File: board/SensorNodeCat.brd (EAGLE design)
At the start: 45.7 x 24.1 mm, 18 parts, among them J1 JP5E

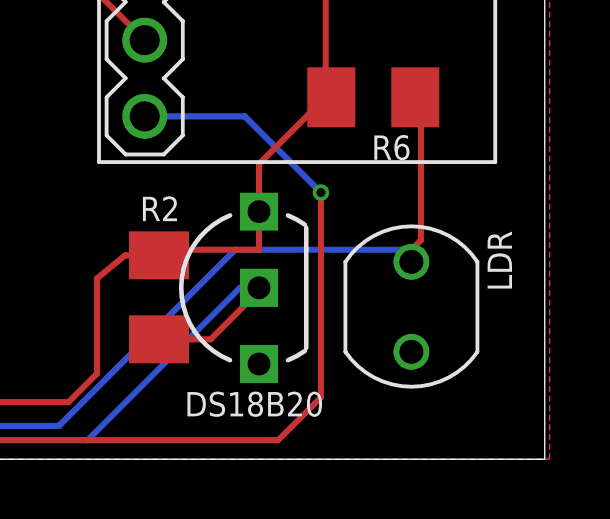
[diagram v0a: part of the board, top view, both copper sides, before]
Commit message: add resistor parallel to LDR
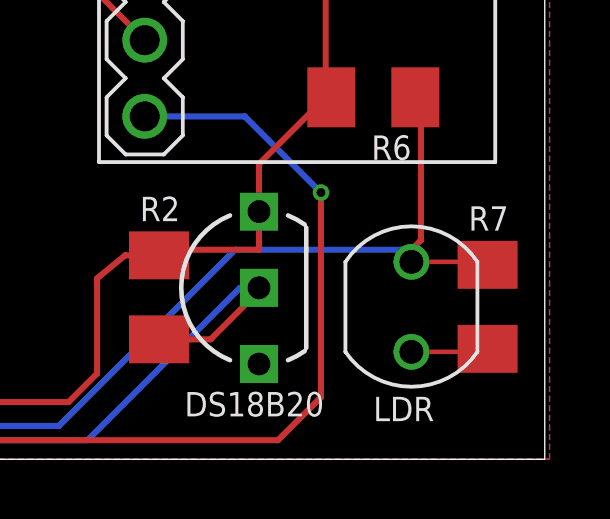
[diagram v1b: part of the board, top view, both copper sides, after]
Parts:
- added R7: 39k, rcl:M1206
- C4: value 1nF -> 100nF
- R6: value 10k -> 100k
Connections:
- net GND: now also R7.1
- net N$5: now also R7.2
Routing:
- net N$5: track 31.1 -> 33.7 mm
- net GND: track 0.00 -> 2.58 mm
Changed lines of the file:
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@@
 <?xml version="1.0" encoding="utf-8"?>
 <!DOCTYPE eagle SYSTEM "eagle.dtd">
-<eagle version="9.5.2">
+<eagle version="9.6.2">
 <drawing>
 <settings>
@@
 <attribute name="VALUE" x="12.22375" y="6.985" size="0.6096" layer="27" ratio="15" rot="R90"/>
 </element>
-<element name="C4" library="rcl" library_urn="urn:adsk.eagle:library:334" package="C1206" package3d_urn="urn:adsk.eagle:package:23618/2" value="1nF" x="14.76375" y="7.62" smashed="yes" rot="R90">
+<element name="C4" library="rcl" library_urn="urn:adsk.eagle:library:334" package="C1206" package3d_urn="urn:adsk.eagle:package:23618/2" value="100nF" x="14.76375" y="7.62" smashed="yes" rot="R90">
 <attribute name="NAME" x="15.39875" y="10.95375" size="0.8128" layer="25" ratio="20" rot="R180"/>
 <attribute name="SPICEPREFIX" value="C" x="14.76375" y="7.62" size="1.778" layer="27" rot="R90" display="off"/>
@@
 <attribute name="VALUE" x="-0.381" y="22.225" size="1.27" layer="27" ratio="10" rot="R270"/>
 </element>
-<element name="R6" library="rcl" library_urn="urn:adsk.eagle:library:334" package="M1206" package3d_urn="urn:adsk.eagle:package:23566/2" value="10k" x="40.005" y="12.065" smashed="yes" rot="R180">
+<element name="R6" library="rcl" library_urn="urn:adsk.eagle:library:334" package="M1206" package3d_urn="urn:adsk.eagle:package:23566/2" value="100k" x="40.005" y="12.065" smashed="yes" rot="R180">
 <attribute name="NAME" x="41.275" y="10.795" size="0.8128" layer="25" ratio="20" rot="R180"/>
 <attribute name="SPICEPREFIX" value="R" x="40.005" y="12.065" size="1.778" layer="27" rot="R180" display="off"/>
@@
 </element>
 <element name="LDR" library="thomo" package="GL55" value="LDR-GL55XX" x="41.275" y="5.08" smashed="yes" rot="R270">
-<attribute name="NAME" x="43.815" y="7.62" size="0.8128" layer="25" ratio="20" rot="R270"/>
+<attribute name="NAME" x="40.005" y="1.27" size="0.8128" layer="25" ratio="20"/>
 <attribute name="VALUE" x="37.465" y="7.62" size="1.27" layer="27" rot="R270"/>
+</element>
+<element name="R7" library="rcl" library_urn="urn:adsk.eagle:library:334" package="M1206" package3d_urn="urn:adsk.eagle:package:23566/2" value="39k" x="43.815" y="5.08" smashed="yes" rot="R90">
+<attribute name="NAME" x="43.18" y="7.62" size="0.8128" layer="25" ratio="20"/>
+<attribute name="SPICEPREFIX" value="R" x="43.815" y="5.08" size="1.778" layer="27" rot="R90" display="off"/>
+<attribute name="VALUE" x="46.355" y="3.81" size="1.27" layer="27" rot="R90"/>
 </element>
 </elements>
@@
 <contactref element="SV1" pad="7"/>
 <contactref element="LDR" pad="2"/>
+<contactref element="R7" pad="1"/>
+<wire x1="43.815" y1="3.68" x2="43.715" y2="3.58" width="0.1524" layer="1"/>
+<wire x1="43.715" y1="3.58" x2="41.275" y2="3.58" width="0.1524" layer="1"/>
 </signal>
 <signal name="+3V3">
@@
 <wire x1="41.275" y1="6.58" x2="41.275" y2="6.985" width="0.2032" layer="1"/>
 <wire x1="41.5925" y1="12.065" x2="41.405" y2="12.065" width="0.2032" layer="1"/>
+<contactref element="R7" pad="2"/>
+<wire x1="41.275" y1="6.58" x2="43.715" y2="6.58" width="0.1524" layer="1"/>
+<wire x1="43.715" y1="6.58" x2="43.815" y2="6.48" width="0.1524" layer="1"/>
 </signal>
 </signals>

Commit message: add LDR and text to PCB
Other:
- board text added: "+V"
- board text added: "3V3"
- board text added: "SensorNodeCat v1.1 01/2021 (c) ThoMo"
- board text removed: "SensorNodeCat v1.0 ThoMo 10/2020"
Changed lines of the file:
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@@
 <setting verticaltext="up"/>
 </settings>
-<grid distance="0.025" unitdist="inch" unit="inch" style="lines" multiple="2" display="yes" altdistance="5" altunitdist="mil" altunit="mil"/>
+<grid distance="0.0125" unitdist="inch" unit="inch" style="lines" multiple="2" display="yes" altdistance="5" altunitdist="mil" altunit="mil"/>
 <layers>
-<layer number="1" name="Top" color="4" fill="1" visible="yes" active="yes"/>
+<layer number="1" name="Top" color="4" fill="1" visible="no" active="yes"/>
 <layer number="2" name="Route2" color="1" fill="3" visible="no" active="no"/>
 <layer number="3" name="Route3" color="4" fill="3" visible="no" active="no"/>
@@
 <layer number="14" name="Route14" color="1" fill="6" visible="no" active="no"/>
 <layer number="15" name="Route15" color="4" fill="6" visible="no" active="no"/>
-<layer number="16" name="Bottom" color="1" fill="1" visible="yes" active="yes"/>
+<layer number="16" name="Bottom" color="1" fill="1" visible="no" active="yes"/>
 <layer number="17" name="Pads" color="2" fill="1" visible="yes" active="yes"/>
-<layer number="18" name="Vias" color="2" fill="1" visible="yes" active="yes"/>
-<layer number="19" name="Unrouted" color="6" fill="1" visible="yes" active="yes"/>
-<layer number="20" name="Dimension" color="24" fill="1" visible="yes" active="yes"/>
-<layer number="21" name="tPlace" color="7" fill="1" visible="yes" active="yes"/>
+<layer number="18" name="Vias" color="2" fill="1" visible="no" active="yes"/>
+<layer number="19" name="Unrouted" color="6" fill="1" visible="no" active="yes"/>
+<layer number="20" name="Dimension" color="24" fill="1" visible="no" active="yes"/>
+<layer number="21" name="tPlace" color="7" fill="1" visible="no" active="yes"/>
 <layer number="22" name="bPlace" color="7" fill="1" visible="yes" active="yes"/>
-<layer number="23" name="tOrigins" color="15" fill="1" visible="yes" active="yes"/>
-<layer number="24" name="bOrigins" color="15" fill="1" visible="yes" active="yes"/>
-<layer number="25" name="tNames" color="7" fill="1" visible="yes" active="yes"/>
+<layer number="23" name="tOrigins" color="15" fill="1" visible="no" active="yes"/>
+<layer number="24" name="bOrigins" color="15" fill="1" visible="no" active="yes"/>
+<layer number="25" name="tNames" color="7" fill="1" visible="no" active="yes"/>
 <layer number="26" name="bNames" color="7" fill="1" visible="yes" active="yes"/>
 <layer number="27" name="tValues" color="7" fill="1" visible="no" active="yes"/>
@@
 <layer number="37" name="tTest" color="7" fill="1" visible="no" active="yes"/>
 <layer number="38" name="bTest" color="7" fill="1" visible="no" active="yes"/>
-<layer number="39" name="tKeepout" color="4" fill="11" visible="yes" active="yes"/>
-<layer number="40" name="bKeepout" color="1" fill="11" visible="yes" active="yes"/>
-<layer number="41" name="tRestrict" color="4" fill="10" visible="yes" active="yes"/>
-<layer number="42" name="bRestrict" color="1" fill="10" visible="yes" active="yes"/>
+<layer number="39" name="tKeepout" color="4" fill="11" visible="no" active="yes"/>
+<layer number="40" name="bKeepout" color="1" fill="11" visible="no" active="yes"/>
+<layer number="41" name="tRestrict" color="4" fill="10" visible="no" active="yes"/>
+<layer number="42" name="bRestrict" color="1" fill="10" visible="no" active="yes"/>
 <layer number="43" name="vRestrict" color="2" fill="10" visible="no" active="yes"/>
 <layer number="44" name="Drills" color="7" fill="1" visible="no" active="yes"/>
-<layer number="45" name="Holes" color="7" fill="1" visible="yes" active="yes"/>
+<layer number="45" name="Holes" color="7" fill="1" visible="no" active="yes"/>
 <layer number="46" name="Milling" color="3" fill="1" visible="no" active="yes"/>
 <layer number="47" name="Measures" color="7" fill="1" visible="no" active="yes"/>
@@
 <plain>
 <wire x1="0" y1="17.145" x2="0" y2="5.715" width="0" layer="20"/>
-<text x="23.8125" y="19.20875" size="0.8128" layer="25" ratio="20">GND</text>
-<text x="21.74875" y="19.20875" size="0.8128" layer="25" ratio="20">RX</text>
-<text x="19.05" y="19.20875" size="0.8128" layer="25" ratio="20">TX</text>
-<text x="13.6525" y="19.20875" size="0.8128" layer="25" ratio="20">GP0</text>
-<text x="39.84625" y="9.04875" size="1.016" layer="26" ratio="20" rot="MR90">SensorNodeCat v1.0
-ThoMo
-10/2020</text>
-<text x="16.35125" y="19.20875" size="0.8128" layer="25" ratio="20">RST</text>
+<text x="23.8125" y="19.20875" size="1.016" layer="25" ratio="20">GND</text>
+<text x="21.74875" y="19.20875" size="1.016" layer="25" ratio="20">RX</text>
+<text x="19.05" y="19.20875" size="1.016" layer="25" ratio="20">TX</text>
+<text x="13.0175" y="19.20875" size="1.016" layer="25" ratio="20">GP0</text>
+<text x="38.57625" y="9.36625" size="1.27" layer="26" ratio="20" rot="MR90">SensorNodeCat
+v1.1 01/2021
+(c) ThoMo </text>
+<text x="16.35125" y="19.20875" size="1.016" layer="25" ratio="20">RST</text>
 <wire x1="0" y1="0" x2="45.72" y2="0" width="0" layer="20"/>
 <wire x1="45.72" y1="0" x2="45.72" y2="24.13" width="0" layer="20"/>
 <wire x1="45.72" y1="24.13" x2="0" y2="24.13" width="0" layer="20"/>
 <wire x1="0" y1="24.13" x2="0" y2="0" width="0" layer="20"/>
+<wire x1="0.635" y1="21.59" x2="0.635" y2="10.16" width="0.1524" layer="25"/>
+<wire x1="0.635" y1="8.89" x2="0.635" y2="2.54" width="0.1524" layer="25"/>
+<text x="3.4925" y="23.65375" size="1.016" layer="25" ratio="20" rot="R180">+V</text>
+<text x="1.27" y="0.47625" size="1.016" layer="25" ratio="20">GND</text>
+<text x="30.48" y="19.52625" size="1.016" layer="25" ratio="20" rot="R180">3V3</text>
+<text x="30.48" y="16.98625" size="1.016" layer="25" ratio="20" rot="R180">GND</text>
+<text x="1.74625" y="23.33625" size="1.016" layer="26" ratio="20" rot="MR180">+V</text>
+<text x="1.42875" y="2.06375" size="1.016" layer="26" ratio="20" rot="MR180">GND</text>
+<text x="33.81375" y="19.52625" size="1.016" layer="26" ratio="20" rot="MR180">3V3</text>
+<text x="33.81375" y="16.98625" size="1.016" layer="26" ratio="20" rot="MR180">GND</text>
+<wire x1="4.445" y1="21.59" x2="4.445" y2="10.16" width="0.1524" layer="26"/>
+<wire x1="4.445" y1="8.89" x2="4.445" y2="2.54" width="0.1524" layer="26"/>
 </plain>
 <attributes>
